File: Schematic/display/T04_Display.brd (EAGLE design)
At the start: 76.3 x 50.8 mm, 57 parts

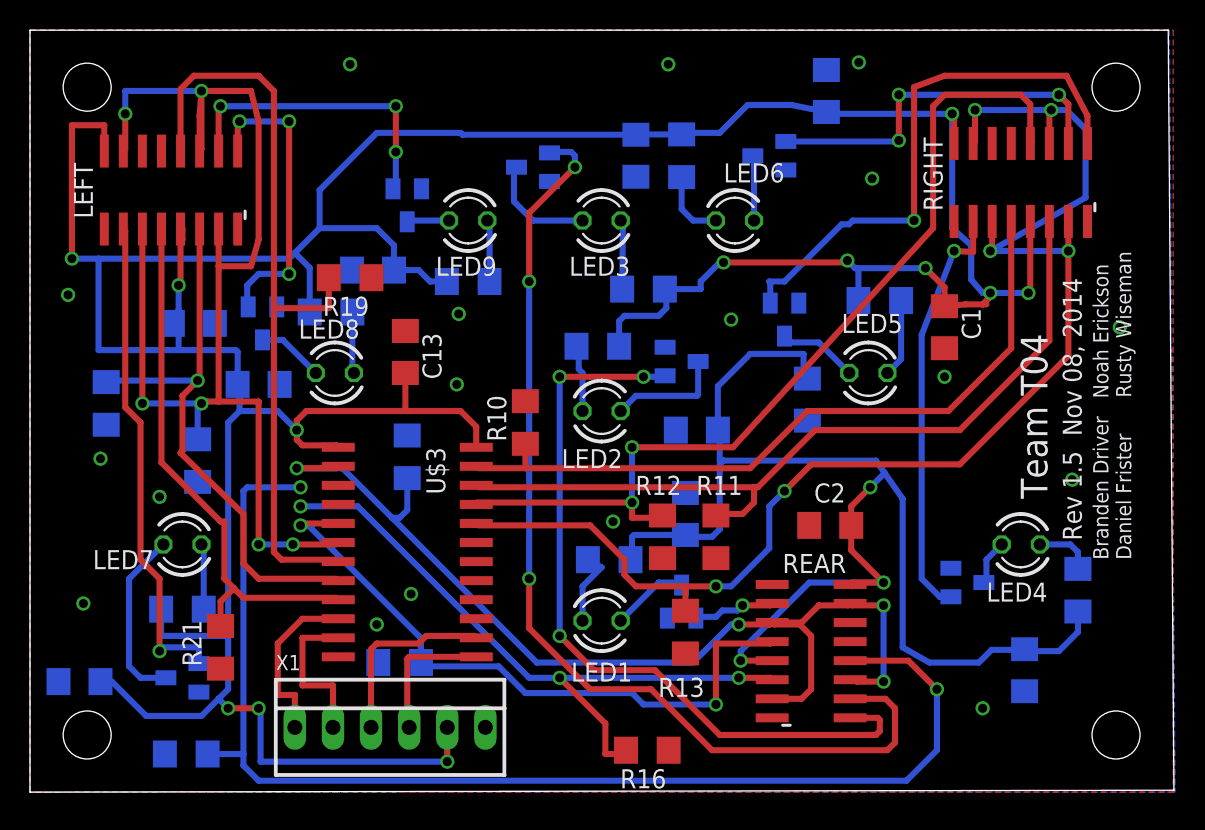
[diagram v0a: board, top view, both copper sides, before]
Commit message: Display w/ 7-pin molex
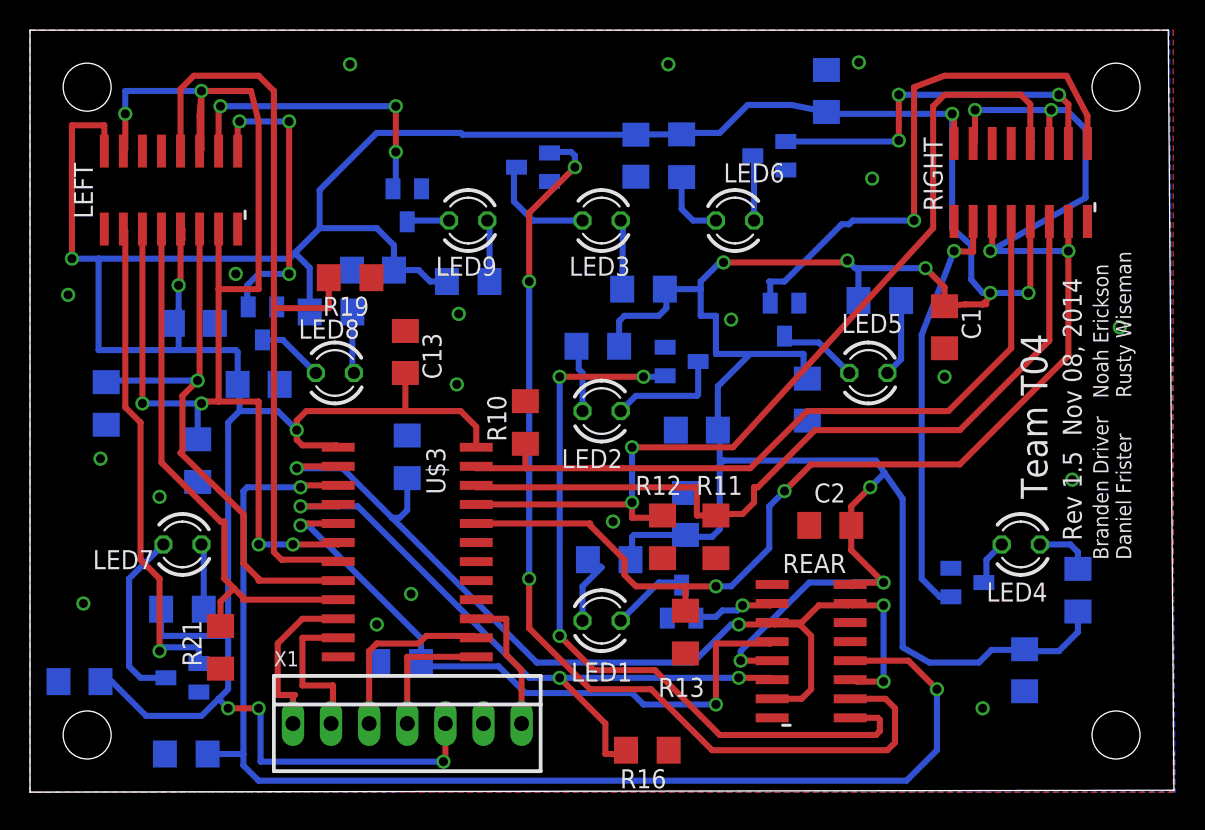
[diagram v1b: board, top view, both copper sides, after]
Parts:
- X1: value (none) -> 22-23-2071; device con-molex:22-23-2061 -> con-molex:22-23-2071
- moved X1 1.17 mm to (25.1, 4.57)
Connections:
- new net MUXENABLE: U$3.15, X1.7
- net GND: no longer U$3.15
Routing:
- net MUXENABLE: track 0.00 -> 9.41 mm
- net VDD: track 349.0 -> 357.0 mm
- net LS2: track 44.2 -> 46.9 mm
- net LS3: track 82.9 -> 85.3 mm
- net BRES: track 82.7 -> 84.9 mm
